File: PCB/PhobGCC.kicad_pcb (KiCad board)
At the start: 2 copper layers, 125.5 x 72.9 mm, 44 parts, among them J1 Conn_01x06_Female, J2 Conn_01x04_Female, J3 Conn_01x01_Male, J4 Conn_01x01_Male, J6 10118194-0001LF, SW1 A, SW10 Dup, SW11 Dright, SW12 Ddown, SW2 B, SW3 X, SW4 Y, SW5 Start, SW6 L, SW7 R, SW8 1825027-5, SW9 Dleft, U1 Teensy3.2, U2 Stickbox_Assembly

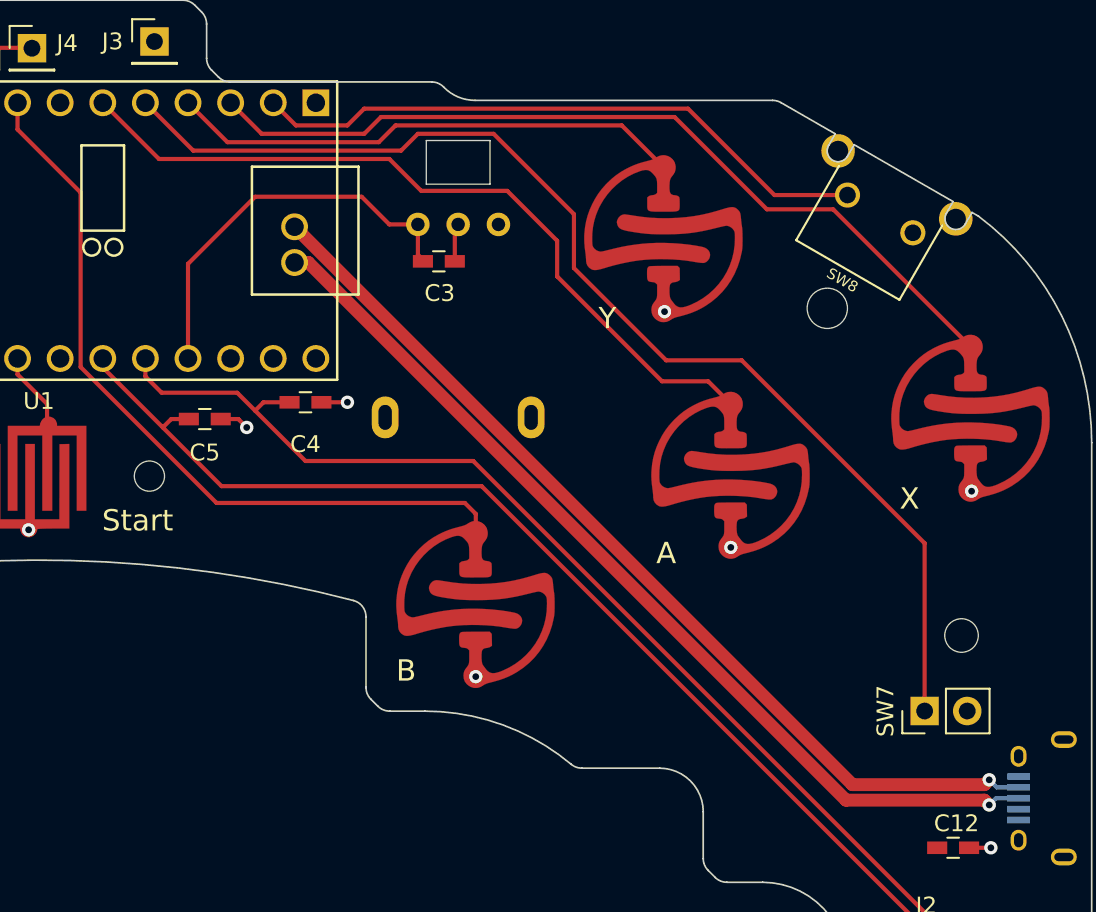
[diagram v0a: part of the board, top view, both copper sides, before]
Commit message: Changed pinout to match board made by jlc, these boards worked except that the usb data pads didn't line up. Something still wrong with affine transforms. Need to play around with filtering and PODE emulation to get good behavior, right now cannot use kalman velocity because it falls to 0 in the mid range.
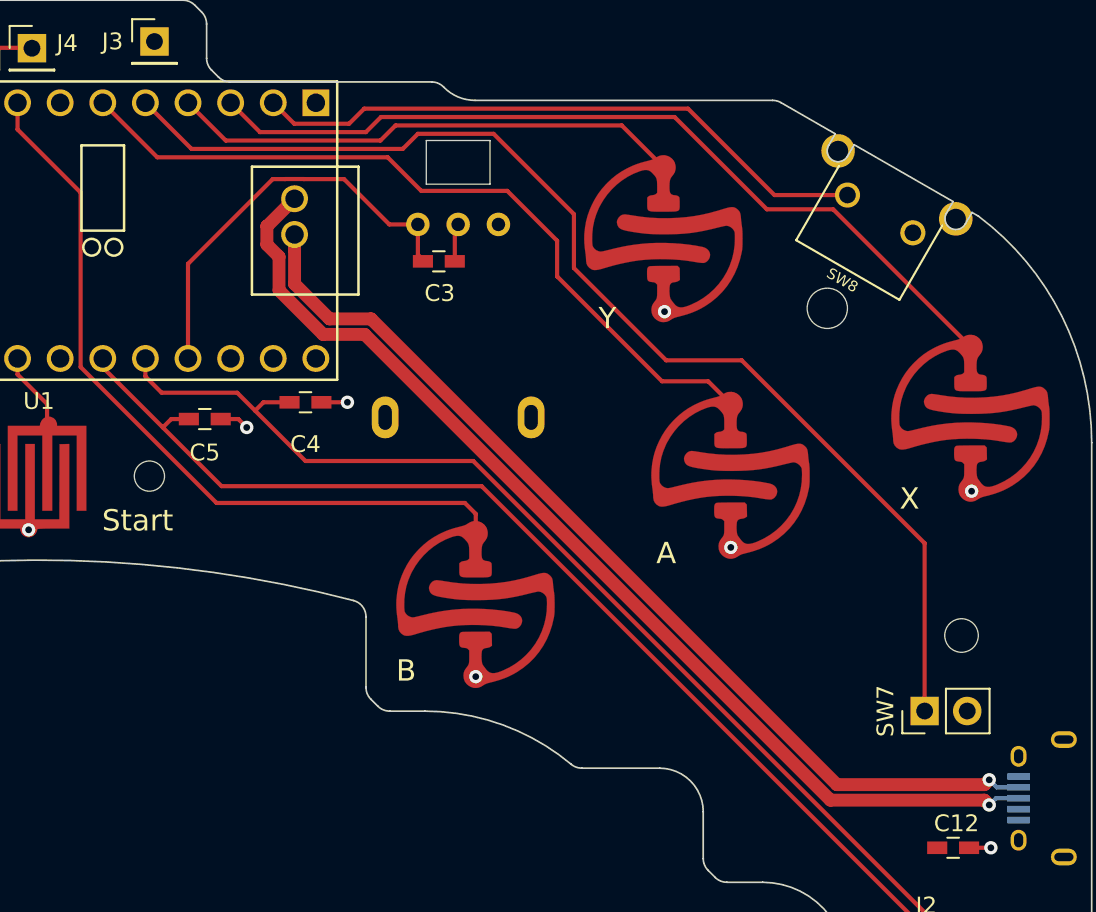
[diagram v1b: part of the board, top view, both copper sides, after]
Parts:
- U1: footprint Teensy:Teensy30_31_32_USB -> teensy:Teensy30_31_32_USB
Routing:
- net /D+: track 56.7 -> 63.4 mm
- net /D-: track 57.2 -> 58.8 mm
- net /Ranalog: track 23.9 -> 24.8 mm

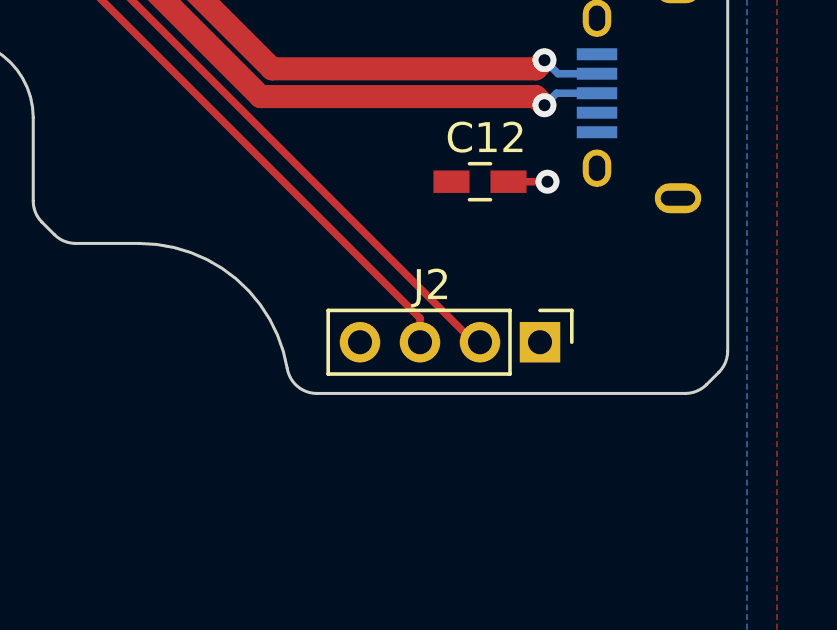
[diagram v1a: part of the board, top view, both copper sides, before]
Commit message: Added use of bounce library to manage starting calibrations. Updated the schematic moving the c-stick connector to the bottom.
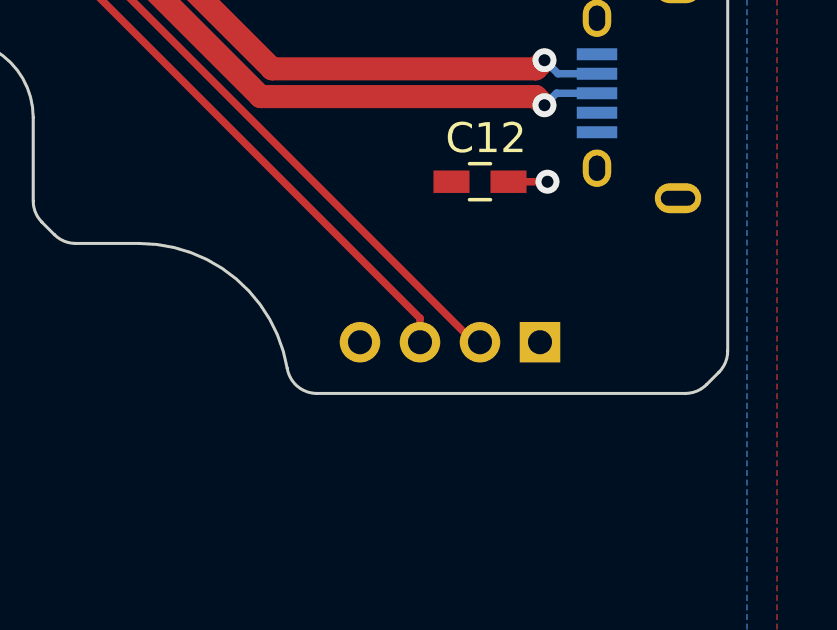
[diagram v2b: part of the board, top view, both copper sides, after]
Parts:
- J2: moved to B.Cu
- turned J2 to 90 degrees

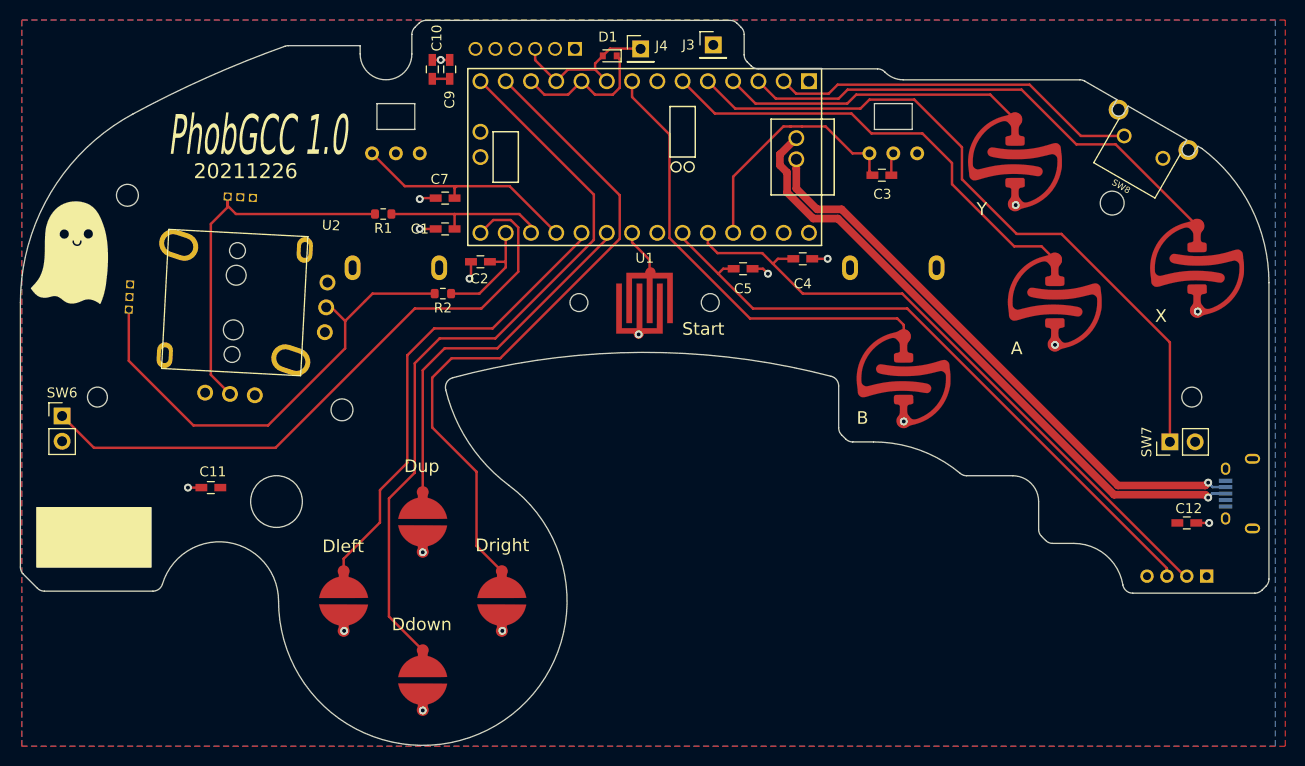
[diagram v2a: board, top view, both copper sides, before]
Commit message: Updated PCB to version 1.1, small fixes
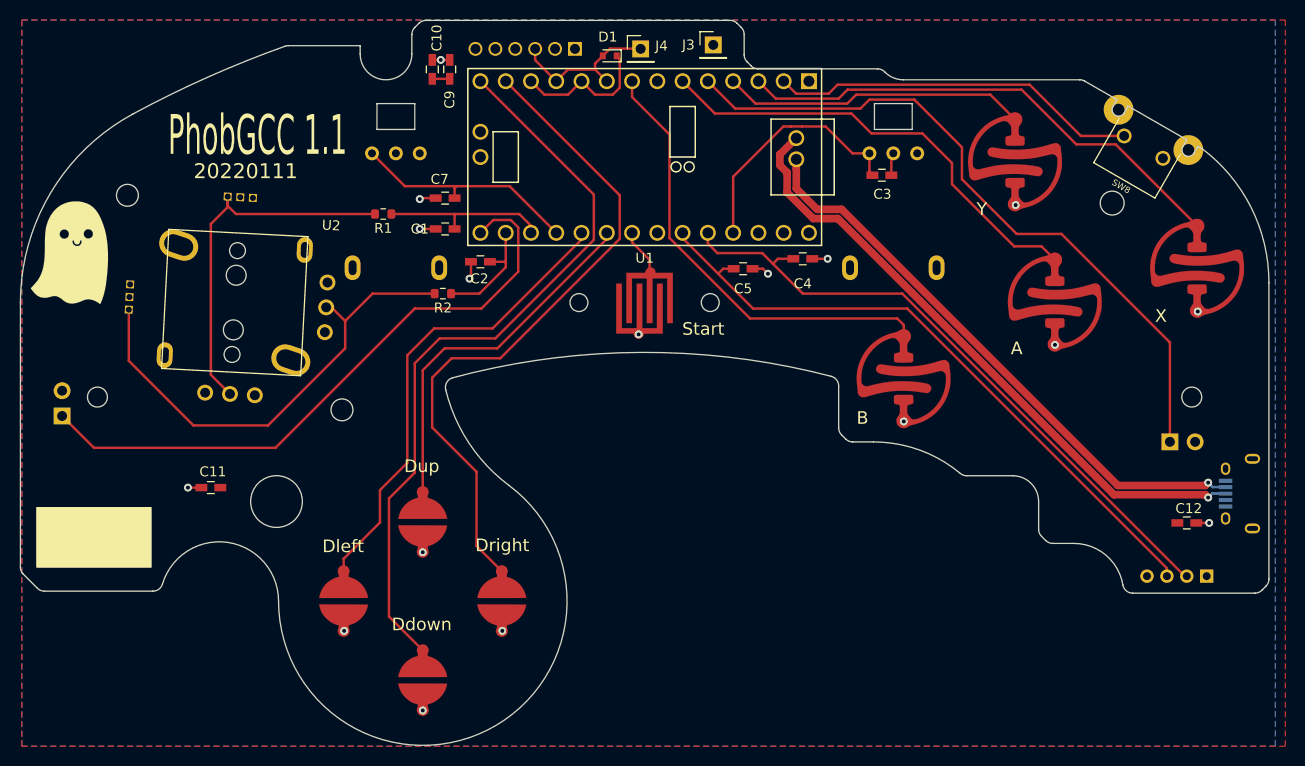
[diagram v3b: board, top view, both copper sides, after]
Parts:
- SW6, SW7: moved to B.Cu
- turned SW7 to 270 degrees
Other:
- board text added: "20220111"
- board text added: "PhobGCC 1.1"
- board text removed: "20211226"
- board text removed: "PhobGCC 1.0"

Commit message: Updated layout so the LED pin doesn't get used, added link to wiki in readme.
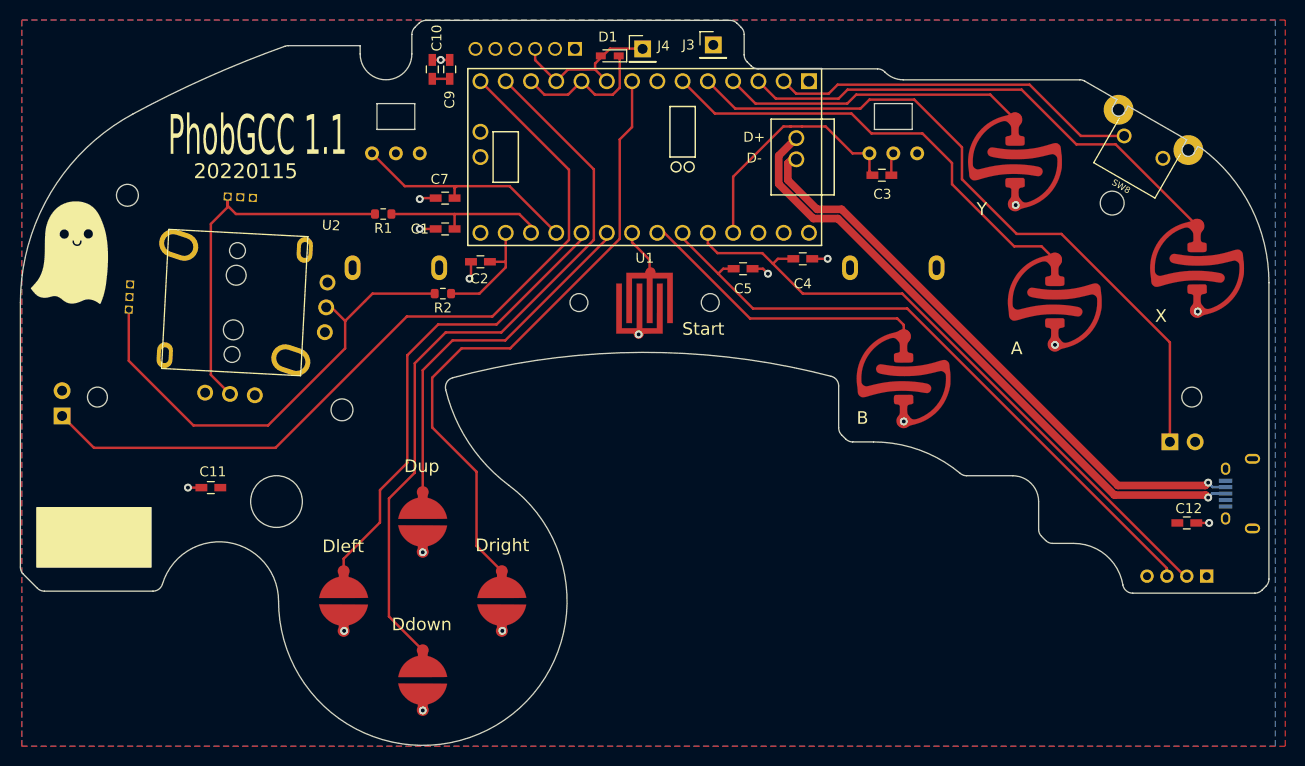
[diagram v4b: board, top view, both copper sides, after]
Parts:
- C1, C11, C12, C2, C3, C4, C5, C7, C9: value C -> 2200p
- C10: value C -> 0.1u
- D1: footprint Diode_SMD:D_SOD-523 -> Gamecube MB:D_SOD-523_large_pads
- R1, R2: value R -> 10k
- U2: value Stickbox_Assembly -> 2x DRV5053CAQLPGM Hall Effect Sensors
- moved J4 0.20 mm to (112.4, 52.9)
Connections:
- U1 pad 13: /Dright -> /Ddown
- U1 pad 14: /Ddown -> /L
- U1 pad 20: /L -> Net-(U1-Pad20)
- U1 pad 27: Net-(U1-Pad27) -> /B
- U1 pad 8: /B -> /Dright
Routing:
- net /L: track 63.6 -> 80.6 mm
- net /B: track 45.6 -> 29.8 mm
- net /Dright: track 67.6 -> 63.3 mm
- net /Ddown: track 75.1 -> 74.1 mm
- net /D-: track 58.8 -> 59.7 mm
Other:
- board text added: "20220115"
- board text removed: "20220111"

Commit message: Changed the internal reference voltage check to update every loop. Changed the PCB to use a 2.5V regulator to power the hall effect sensors and pots as well as act as the ADC reference.
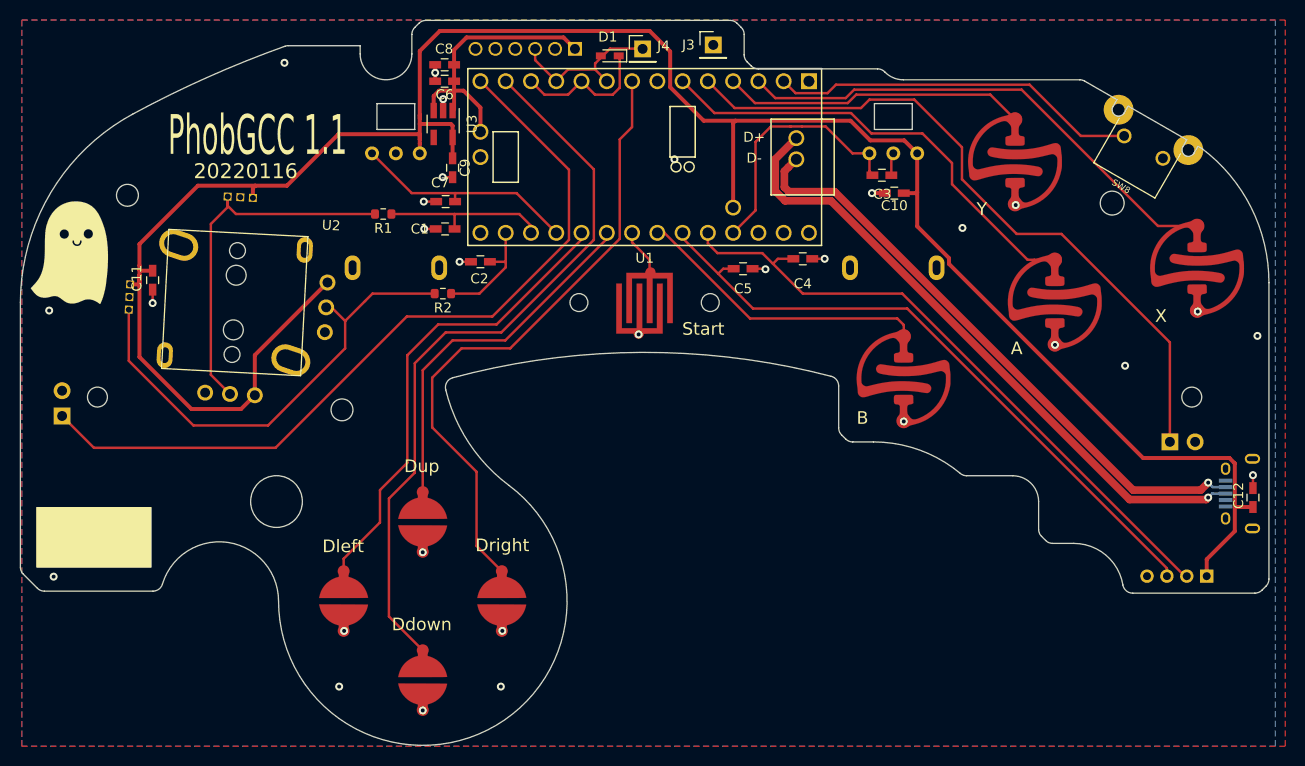
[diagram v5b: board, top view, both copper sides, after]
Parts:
- added C6: 2200p, Capacitors_SMD:C_0603_HandSoldering, F.Cu at (92.5, 56.1)
- added C8: 1u, Capacitors_SMD:C_0603_HandSoldering, F.Cu at (92.5, 54.5)
- added U3: XC6220B331MR, TO_SOT_Packages_SMD:SOT-23-5_HandSoldering, F.Cu at (92.3, 60.5)
- C10: value 0.1u -> 2200p
- C9: value 2200p -> 1u
- moved C10 48.1 mm to (137.7, 67.4), turned to 180 degrees
- moved C11 21.7 mm to (63.1, 76.2), turned to 270 degrees
- moved C9 9.89 mm to (93.3, 64.8), turned to 270 degrees
- moved C12 7.12 mm to (173.8, 98.0), turned to 90 degrees
- moved C7 0.35 mm to (92.6, 68.2)
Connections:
- C10 pad 1: +3V3 -> +2V5
- C11 pad 1: +3V3 -> +2V5
- C12 pad 1: +3V3 -> +2V5
- C9 pad 1: +3V3 -> +2V5
- J1 pad 2: +5V -> (no net)
- J2 pad 1: +3V3 -> +2V5
- J6 pad 1: Net-(J6-Pad1) -> (no net)
- J6 pad 4: Net-(J6-Pad4) -> (no net)
- RV1 pad 1: +3V3 -> +2V5
- RV2 pad 1: +3V3 -> +2V5
- U1 pad 20: Net-(U1-Pad20) -> (no net)
- U1 pad 31: +3V3 -> (no net)
- U1 pad 32: Net-(U1-Pad32) -> (no net)
- U1 pad 33: Net-(U1-Pad33) -> (no net)
- U1 pad 7: Net-(U1-Pad7) -> (no net)
- U2 pad 1: +3V3 -> +2V5
- U2 pad 15: +3V3 -> +2V5
- U2 pad 18: +3V3 -> +2V5
- U2 pad 4: +3V3 -> +2V5
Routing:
- net +2V5: track 0.00 -> 227.2 mm
- net +3V3: track 1.75 -> 28.8 mm
- net GND: track 15.8 -> 17.0 mm, vias 17 -> 29
- net /D+: track 63.5 -> 64.6 mm
- net /D-: track 59.7 -> 60.8 mm
- net /Ranalog: track 24.8 -> 25.5 mm
- added copper zone on F.Cu, net GND
- removed copper zone on F.Cu, net +3V3
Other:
- board text added: "20220116"
- board text removed: "20220115"

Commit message: Converted PCB files to kicad v6, generated JLC manufacturing files for 1.1 version of the board, moved the old manufacturing files to the v1_20211226.rar file. Changed the way notch snapping is done, only does so at the cardinals now
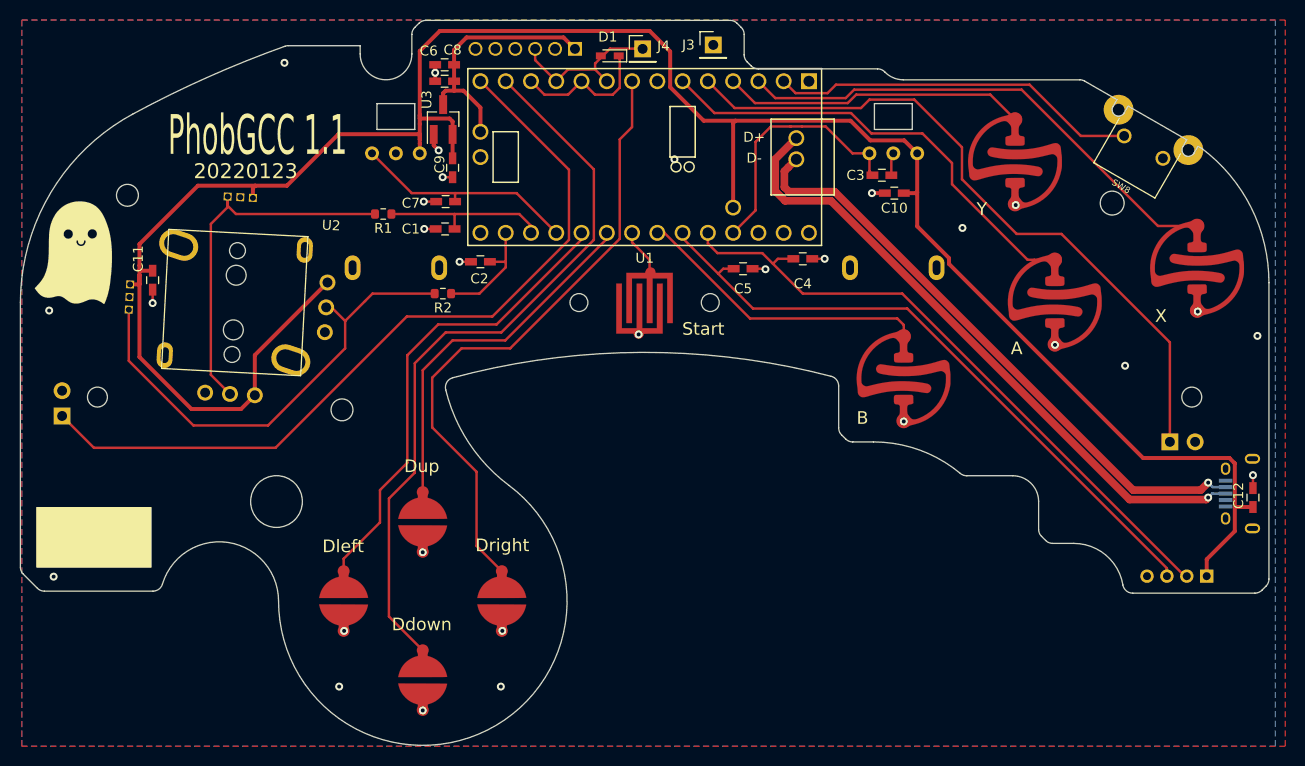
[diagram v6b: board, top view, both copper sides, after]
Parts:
- U3: footprint TO_SOT_Packages_SMD:SOT-23-5_HandSoldering -> Package_TO_SOT_SMD:SOT-23_Handsoldering
- moved U3 0.45 mm to (92.3, 60.0), turned to 90 degrees
- moved G*** 0.40 mm to (55.4, 73.5)
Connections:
- J1 pad 2: (no net) -> +5V
- J6 pad 1: (no net) -> unconnected-(J6-Pad1)
- J6 pad 4: (no net) -> unconnected-(J6-Pad4)
- U1 pad 20: (no net) -> unconnected-(U1-Pad20)
- U1 pad 31: (no net) -> unconnected-(U1-Pad31)
- U1 pad 32: (no net) -> unconnected-(U1-Pad32)
- U1 pad 33: (no net) -> unconnected-(U1-Pad33)
- U1 pad 7: (no net) -> unconnected-(U1-Pad7)
- U3 pad 1: +3V3 -> GND
- U3 pad 2: GND -> +2V5
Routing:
- net +3V3: track 28.8 -> 25.4 mm
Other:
- outline, holes or cut-outs redrawn
- net class Default removed
- net class USB removed
- board text added: "20220123"
- board text removed: "20220116"
